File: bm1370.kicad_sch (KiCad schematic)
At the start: 49 parts, among them U5 MCP1824T-1202E/OT, U6 MCP1824T-0802E, U7 25MHz, U8 BM1370_mode1, U9 SN74AVC4T774

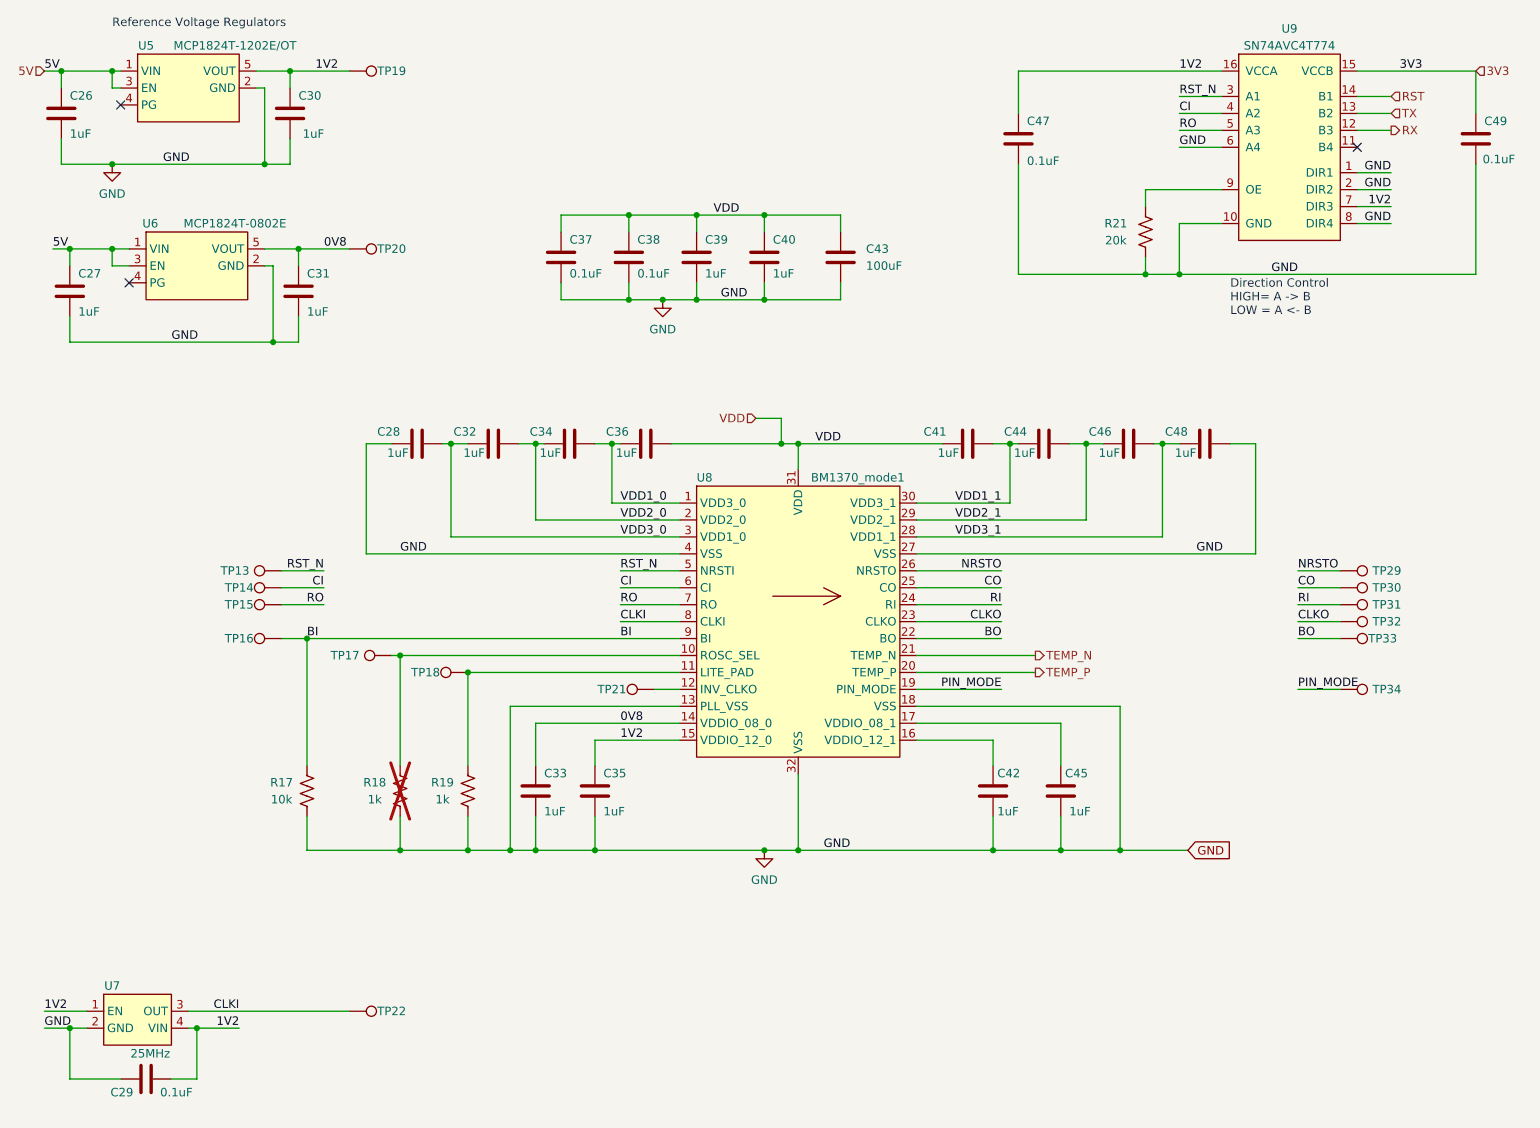
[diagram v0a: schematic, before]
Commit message: added files for model 605 Gamma Kit
Updated sizes for handsoldering kit, added onboard ethernet, cpu heatsink footprint, updated power supply
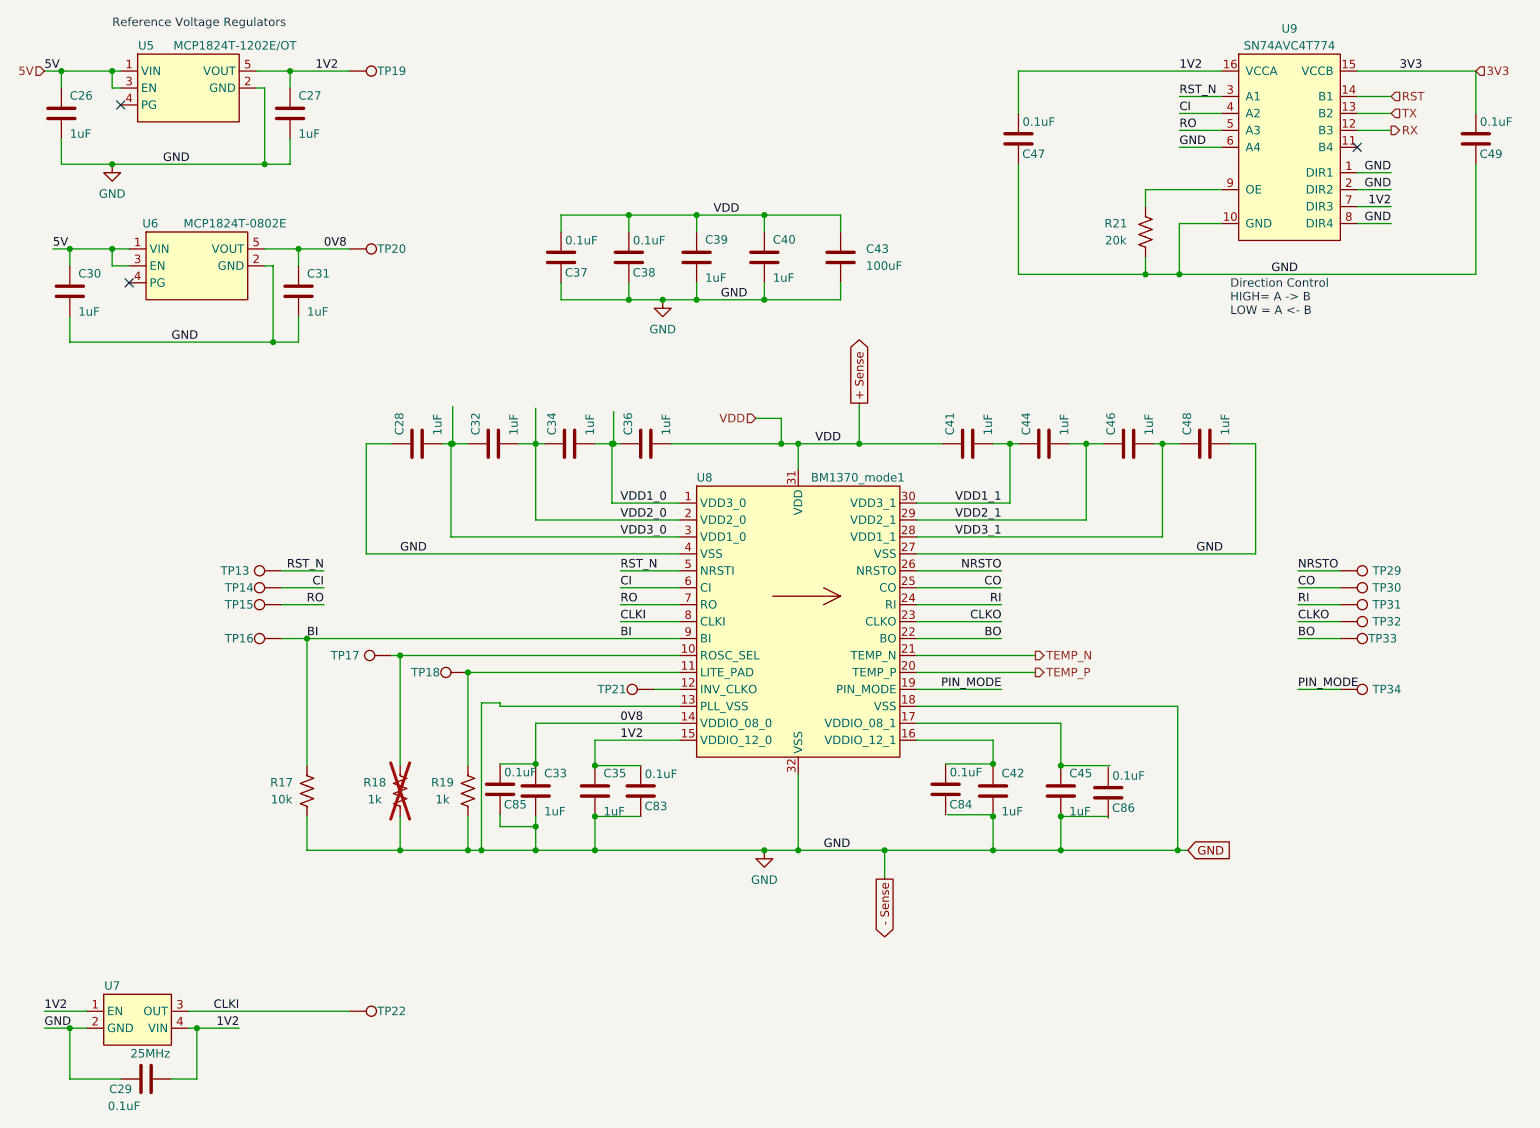
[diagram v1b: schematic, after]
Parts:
- added C83, C84, C85, C86: 0.1uF, Capacitor_SMD:C_1206_3216Metric_Pad1.33x1.80mm_HandSolder, symbol Device:C
- C26, C27, C28, C30, C31, C32, C33, C34, C35, C36, C39, C40, C41, C42, C44, C45, C46, C48: footprint Capacitor_SMD:C_0402_1005Metric -> Capacitor_SMD:C_0805_2012Metric_Pad1.18x1.45mm_HandSolder; DK 587-5514-1-ND -> NMC0805X7R105K25TRPLPFCT-ND; PARTNO EMK105BJ105MV-F -> NMC0805X7R105K25TRPLPF
- C29, C37, C38, C47, C49: footprint Capacitor_SMD:C_0402_1005Metric -> Capacitor_SMD:C_1206_3216Metric_Pad1.33x1.80mm_HandSolder; DK 1276-1234-1-ND -> 4713-GMC31CG104J50NTCT; PARTNO CL05A104KO5NNNC -> GMC31CG104J50NT
- R17: footprint Resistor_SMD:R_0402_1005Metric -> Resistor_SMD:R_0805_2012Metric_Pad1.20x1.40mm_HandSolder; DK 311-10KJRCT-ND -> TNP10.0KABCT-ND; PARTNO RC0402JR-0710KL -> TNPW080510K0BEEA
- R19: footprint Resistor_SMD:R_0402_1005Metric -> Resistor_SMD:R_0805_2012Metric_Pad1.20x1.40mm_HandSolder; DK 311-1.00KLRCT-ND -> TNP1.00KABCT-ND; PARTNO RC0402FR-071KL -> TNPW08051K00BEEA
- R21: footprint Resistor_SMD:R_0402_1005Metric -> Resistor_SMD:R_0805_2012Metric_Pad1.20x1.40mm_HandSolder; DK 311-20.0KLRCT-ND -> TNP20.0KABCT-ND; PARTNO RC0402FR-0720KL -> TNPW080520K0BEEA
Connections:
- net 0V8: now also C85.1
- net 1V2: now also C27.1, C83.1; no longer C30.1
- net 5V: now also C30.1; no longer C27.1
- net GND: now also C83.2, C85.2
- net at C42.1, U8.16 (VDDIO_12_1): now also C84.1
- net VDD renamed + Sense
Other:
- company: (none) -> Oconical
- title: bitaxeGamma -> bitaxeGamma 605 Kit
